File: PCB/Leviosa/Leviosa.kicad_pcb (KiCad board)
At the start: 2 copper layers, 80 x 80 mm, 24 parts, among them Q3 TIP122, Q4 TIP122, U1 LM324, U5 L7805, U6 SS495A

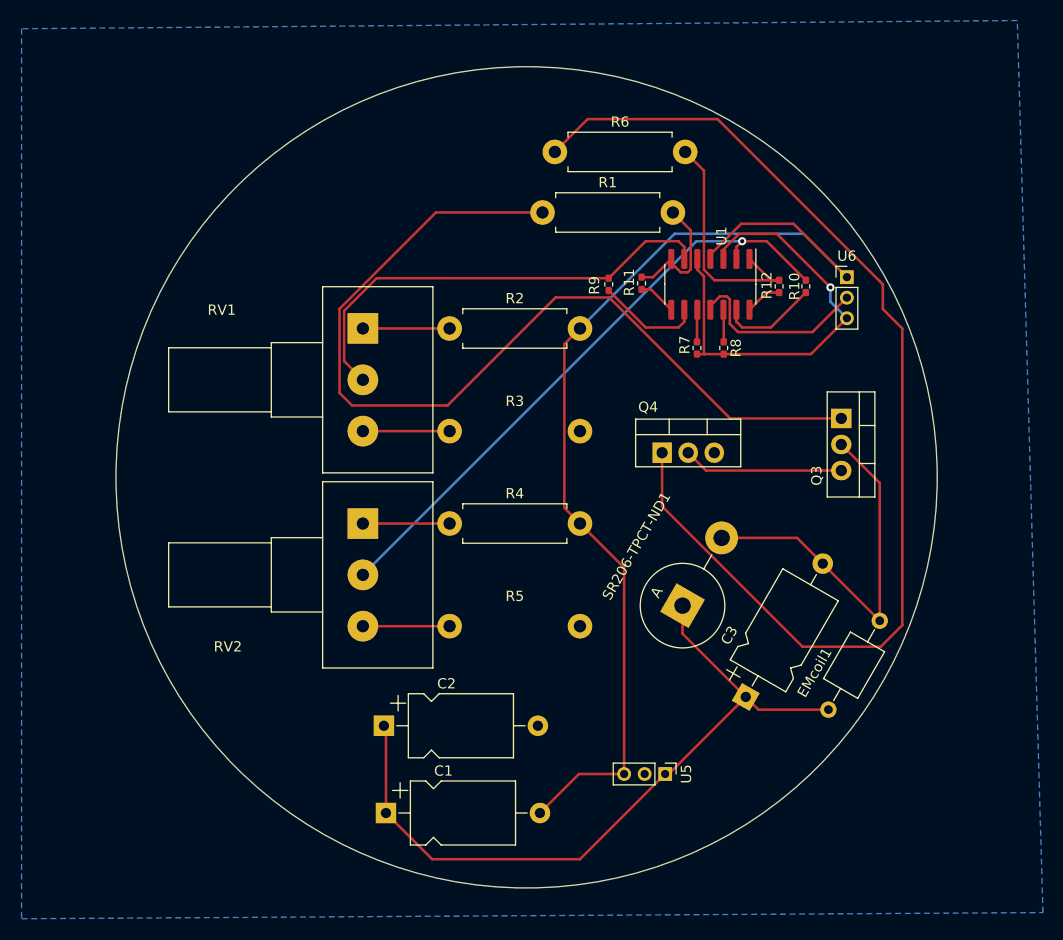
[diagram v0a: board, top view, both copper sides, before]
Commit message: update PCB with some of Jack's feedback
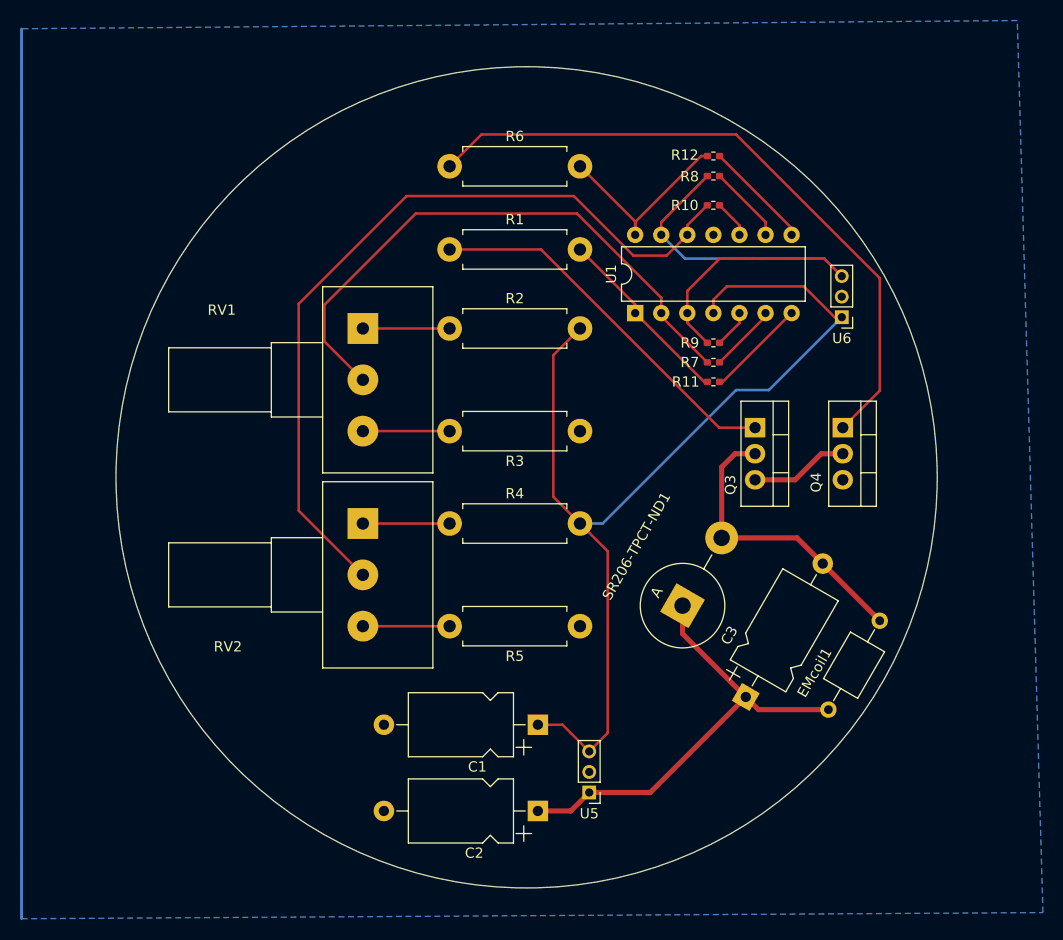
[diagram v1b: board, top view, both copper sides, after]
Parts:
- R3, R5: moved to F.Cu
- U1: footprint Package_SO:SOIC-14_3.9x8.7mm_P1.27mm -> Package_DIP:DIP-14_W7.62mm
- moved Q4 17.8 mm to (195.8, 109.2), turned to -90 degrees
- moved C2 17.1 mm to (166.1, 146.5), turned to 180 degrees
- moved C1 17.1 mm to (166.1, 138.1), turned to 180 degrees
- moved R8 16.8 mm to (183.2, 84.7), turned to 0 degrees
- moved R12 14.2 mm to (183.2, 82.7), turned to 180 degrees
- moved R10 12.0 mm to (183.2, 87.5), turned to 0 degrees
- moved R11 11.9 mm to (183.2, 104.7), turned to 0 degrees
- moved R9 11.7 mm to (183.2, 100.9), turned to 180 degrees
- moved R6 10.3 mm to (157.5, 83.7)
- moved R1 9.74 mm to (157.5, 91.8)
- moved Q3 8.45 mm to (187.3, 109.2)
- moved U1 7.84 mm to (175.6, 98.0), turned to 90 degrees
- moved U5 7.62 mm to (171.1, 144.7), turned to 180 degrees
- moved U6 3.93 mm to (195.7, 98.4), turned to 180 degrees
- moved R7 2.13 mm to (183.2, 102.8), turned to 180 degrees
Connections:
- C1 pad 1: +12V -> /5V
- C1 pad 2: /5V -> GND
- R10 pad 2: Net-(U1D--) -> Net-(U1C-+)
- R11 pad 1: /spare_set_point_trigger -> /set_point_trigger
- R11 pad 2: /set_point_trigger -> /spare_set_point_trigger
- R7 pad 1: Net-(U1C-+) -> Net-(U1B--)
- R7 pad 2: /hall_output -> /set_point
- R8 pad 2: Net-(U1D-+) -> Net-(U1C--)
- R9 pad 1: Net-(U1C--) -> Net-(U1B-+)
- R9 pad 2: /set_point -> /hall_output
- U1 pad 1: /no_magnet_point_trigger -> /set_point_trigger
- U1 pad 12: Net-(U1D-+) -> /no_magnet_point
- U1 pad 13: Net-(U1D--) -> /hall_output
- U1 pad 14: /spare_no_magnet_point_trigger -> /no_magnet_point_trigger
- U1 pad 2: /no_magnet_point -> /set_point
- U1 pad 5: /hall_output -> Net-(U1B-+)
- U1 pad 6: /set_point -> Net-(U1B--)
- U1 pad 7: /set_point_trigger -> /spare_set_point_trigger
- U1 pad 8: /spare_set_point_trigger -> /spare_no_magnet_point_trigger
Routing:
- net Net-(Q3-B): track 90.5 -> 36.9 mm
- net Net-(Q4-B): track 109.1 -> 65.0 mm
- net +12V: track 72.1 -> 44.9 mm
- net GND: track 18.3 -> 0.00 mm
- net /no_magnet_point: track 60.1 -> 78.1 mm, vias 1 -> 0
- net /set_point: track 45.6 -> 57.7 mm
- net Net-(U1D--): track 9.57 -> 0.00 mm
- net /coil_output: track 37.5 -> 29.4 mm
- net /spare_no_magnet_point_trigger: track 3.58 -> 10.6 mm
- net Net-(U1B--): track 0.00 -> 6.66 mm
- net /hall_output: track 43.4 -> 49.9 mm, vias 1 -> 0
- net /spare_set_point_trigger: track 3.71 -> 9.79 mm
- net /transistor1_output: track 15.6 -> 9.60 mm
- net /set_point_trigger: track 12.7 -> 18.2 mm
- net /5V: track 104.9 -> 100.7 mm
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
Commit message: added attiny and load switch. Still need power input.
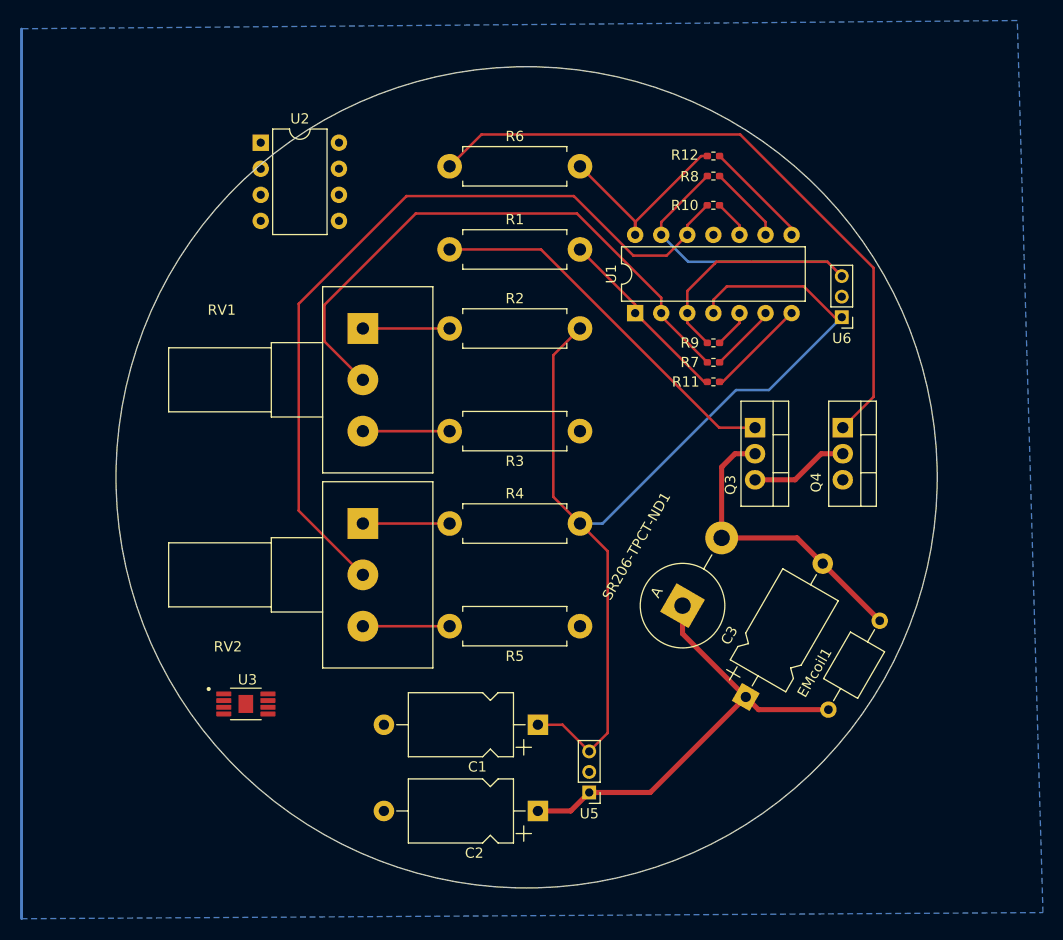
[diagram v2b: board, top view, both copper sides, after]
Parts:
- added U2: ATtiny13A-P, Package_DIP:DIP-8_W7.62mm, F.Cu at (139.1, 81.4)
- added U3: TPS1H200AQDGNRQ1, TPS1H200AQDGNRQ1:SOP65P490X110-9N, F.Cu at (137.7, 136.1)
